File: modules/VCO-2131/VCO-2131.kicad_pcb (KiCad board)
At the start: 2 copper layers, 167.3 x 108.2 mm, 108 parts, among them J1 WQP-PJ398, J10 Conn_Front_Left, J11 Conn_Front_Right, J12 Conn_Back_Right, J13 Conn_Back_Left, J14 Conn_Passthru_Right, J15 Conn_Passthru_Left, J16 Conn_Mid_Right, J17 Conn_Mid_Left, J2 WQP-PJ398, J3 WQP-PJ398, J4 WQP-PJ398, J5 WQP-PJ398, J6 WQP-PJ398, J7 WQP-PJ398, J8 WQP-PJ398, J9 Conn_Eurorack_16, SW5 ON_OFF_ON, U1 L78L05, U2 L79L05, U3 LM4040, U4 SSI2131, U5 TL074, U6 TL074, U7 TL074, U8 CD4013

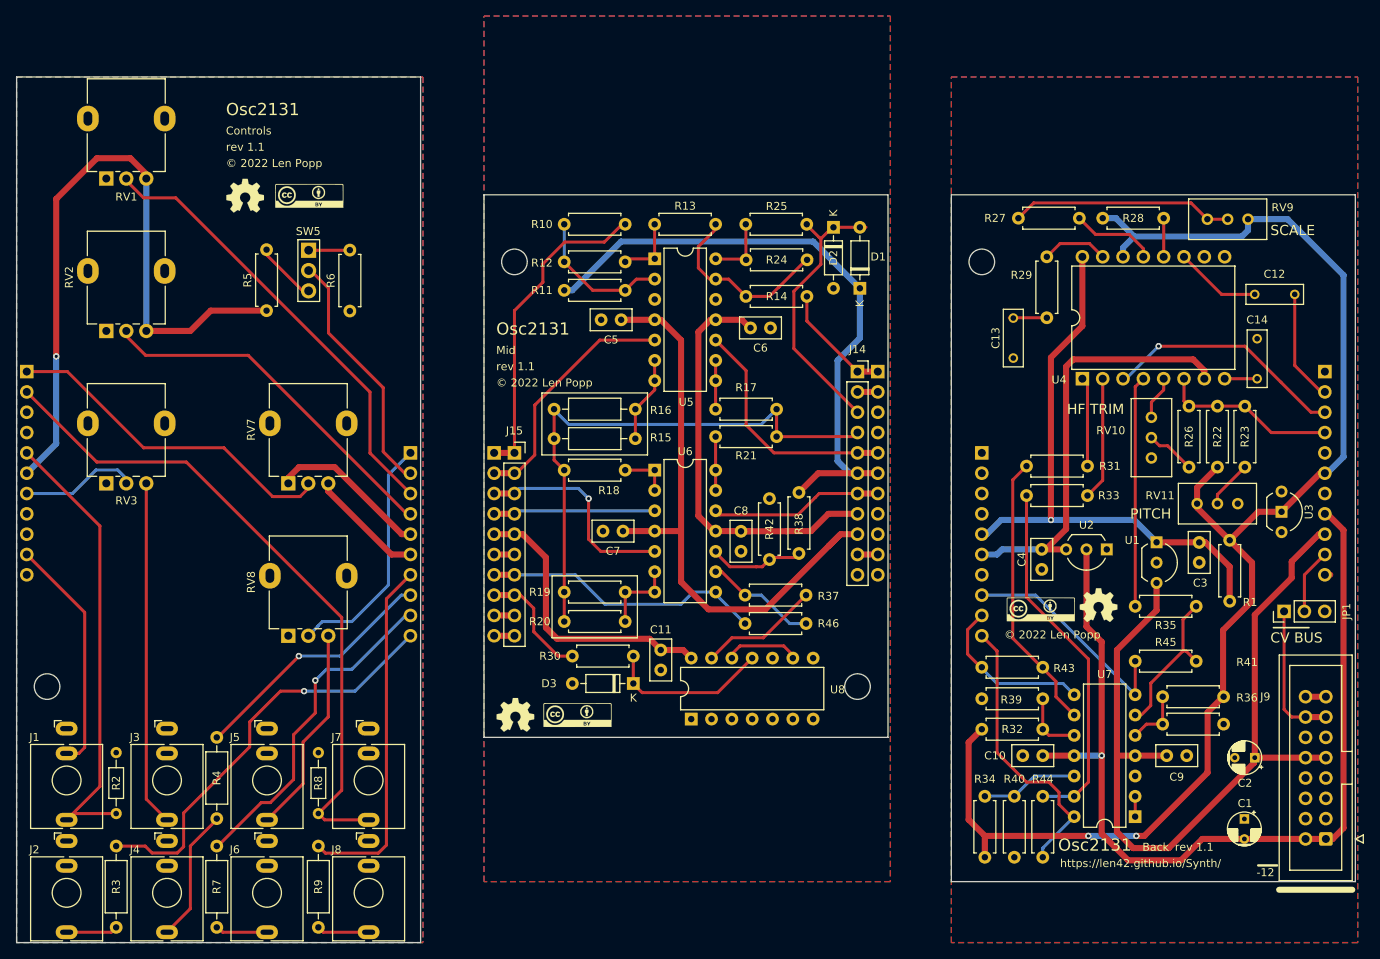
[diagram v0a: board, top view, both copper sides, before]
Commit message: VCO-2131: BOM cleanup, minor circuit changes, and footprint fixes
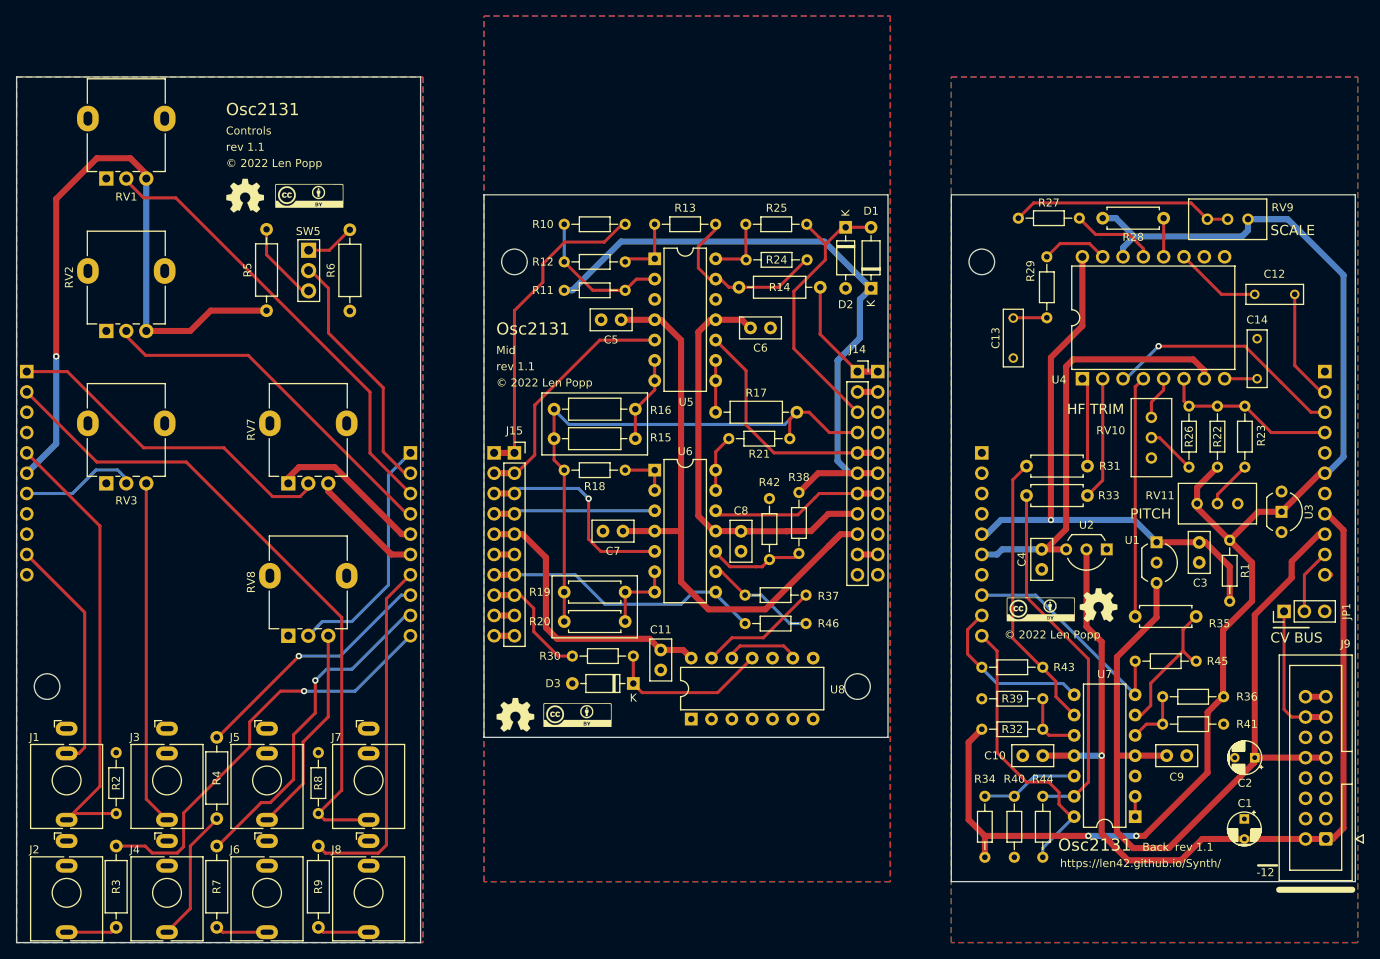
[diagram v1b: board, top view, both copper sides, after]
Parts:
- R1: value 1K -> 470R; footprint -lmp-misc:R_Axial_DIN0207_L6.3mm_D2.5mm_P7.62mm_Horizontal -> -lmp-misc:R_Axial_DIN0204_L3.6mm_D1.6mm_P7.62mm_Horizontal
- R10, R11, R12, R13, R18, R21, R22, R23, R24, R25, R26, R27, R29, R30, R32, R34, R36, R37, R38, R39, R40, R41, R42, R43, R44, R45, R46: footprint -lmp-misc:R_Axial_DIN0207_L6.3mm_D2.5mm_P7.62mm_Horizontal -> -lmp-misc:R_Axial_DIN0204_L3.6mm_D1.6mm_P7.62mm_Horizontal
- R14, R17, R5, R6: footprint -lmp-misc:R_Axial_DIN0207_L6.3mm_D2.5mm_P7.62mm_Horizontal -> -lmp-misc:R_Axial_DIN0207_L6.3mm_D2.5mm_P10.16mm_Horizontal
- R2: value 100K -> 4M7; footprint Resistor_THT:R_Axial_DIN0204_L3.6mm_D1.6mm_P7.62mm_Horizontal -> -lmp-misc:R_Axial_DIN0204_L3.6mm_D1.6mm_P7.62mm_Horizontal
- R8: footprint Resistor_THT:R_Axial_DIN0204_L3.6mm_D1.6mm_P7.62mm_Horizontal -> -lmp-misc:R_Axial_DIN0204_L3.6mm_D1.6mm_P7.62mm_Horizontal
- moved R17 2.57 mm to (121.7, 66.0)
- moved R21 1.67 mm to (120.8, 69.3)
- moved D2 1.52 mm to (127.8, 42.9)
- moved R14 1.44 mm to (114.4, 50.4)
- moved D1 1.40 mm to (130.9, 50.5)
- moved R35 1.27 mm to (171.6, 91.6)
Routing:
- net Net-(R5-Pad2): track 7.39 -> 9.93 mm
- net VREF+: track 337.4 -> 339.4 mm
- net Net-(R6-Pad2): track 4.83 -> 6.22 mm
- net Net-(R35-Pad1): track 18.6 -> 17.3 mm
- net Net-(R35-Pad2): track 28.9 -> 30.1 mm
- net PWM-2131: track 64.6 -> 65.9 mm
- net Net-(R13-Pad1): track 21.9 -> 21.0 mm
- net EXPO-FREQ-2131: track 92.3 -> 93.2 mm

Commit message: VCO-2131: PCB layout tweaks
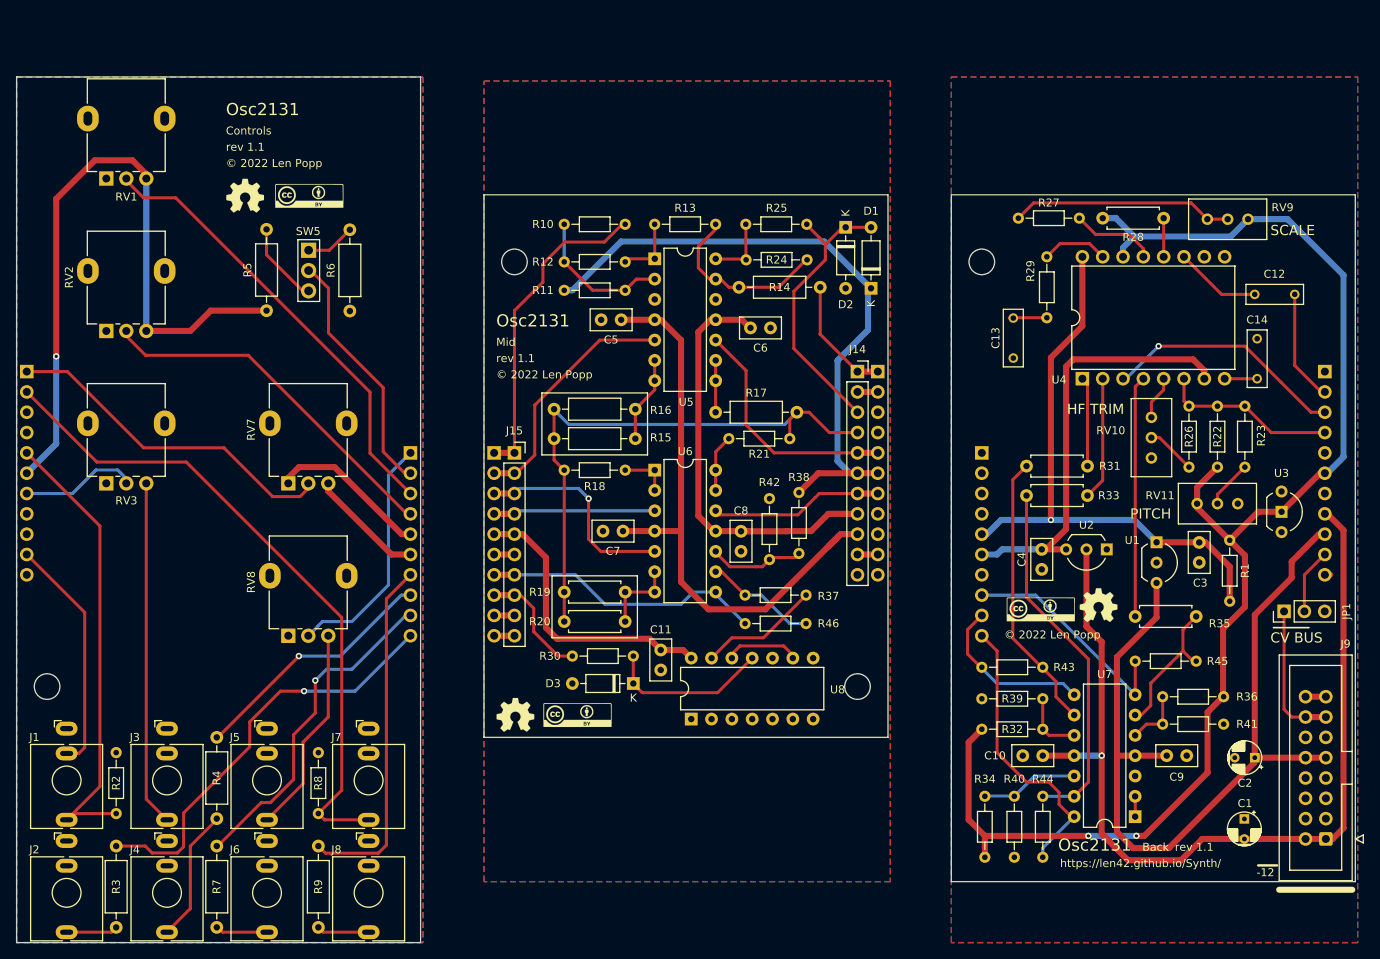
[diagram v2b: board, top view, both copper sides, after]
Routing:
- net VREF+: track 339.4 -> 337.6 mm
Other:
- board text removed: "TODO: Check all resistor footprints"
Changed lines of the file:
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@@
     (property "Value2" "2V5")
     (attr through_hole)
-    (fp_text reference "U3" (at 2.54 -3.43 -90) (layer "F.SilkS")
+    (fp_text reference "U3" (at -2.286 0) (layer "F.SilkS")
       (effects (font (size 1 1) (thickness 0.15)))
     )
@@
   (gr_line (start 191.470001 124.714) (end 140.97 124.714) (layer "Edge.Cuts") (width 0.1524))
   (gr_line (start 24.13 132.334) (end 24.13 24.13) (layer "Edge.Cuts") (width 0.1524))
-  (gr_text "© 2022 Len Popp" (at 84.074 62.357) (layer "F.SilkS")
+  (gr_text "© 2022 Len Popp" (at 84.074 61.341) (layer "F.SilkS")
     (effects (font (size 1 1) (thickness 0.15)) (justify left))
   )
-  (gr_text "Mid" (at 84.074 58.293) (layer "F.SilkS")
+  (gr_text "Mid" (at 84.074 57.277) (layer "F.SilkS")
     (effects (font (size 1 1) (thickness 0.15)) (justify left))
   )
@@
     (effects (font (size 1 1) (thickness 0.15)) (justify left))
   )
-  (gr_text "Osc2131" (at 84.074 55.626) (layer "F.SilkS")
+  (gr_text "Osc2131" (at 84.074 54.61) (layer "F.SilkS")
     (effects (font (size 1.524 1.524) (thickness 0.2286)) (justify left))
   )
@@
     (effects (font (size 1.27 1.27) (thickness 0.2032)) (justify left))
   )
-  (gr_text "rev 1.1" (at 84.074 60.325) (layer "F.SilkS")
-    (effects (font (size 1 1) (thickness 0.15)) (justify left))
-  )
-  (gr_text "TODO: Check all resistor footprints" (at 38.8874 136.652) (layer "Cmts.User")
+  (gr_text "rev 1.1" (at 84.074 59.309) (layer "F.SilkS")
     (effects (font (size 1 1) (thickness 0.15)) (justify left))
   )
@@
   (segment (start 153.416 79.502) (end 163.83 79.502) (width 0.762) (layer "B.Cu") (net 27))
   (segment (start 179.324 78.486) (end 175.768 82.042) (width 0.762) (layer "F.Cu") (net 28))
-  (segment (start 38.354 34.29) (end 40.34 36.276) (width 0.762) (layer "F.Cu") (net 28))
-  (segment (start 173 103.541) (end 174.941 101.6) (width 0.762) (layer "F.Cu") (net 28))
+  (segment (start 177.673 83.947) (end 175.768 82.042) (width 0.762) (layer "F.Cu") (net 28))
+  (segment (start 29.083 59.055) (end 29.083 39.37) (width 0.762) (layer "F.Cu") (net 28))
   (segment (start 174.234 72.898) (end 171.694 75.438) (width 0.762) (layer "F.Cu") (net 28))
+  (segment (start 29.083 39.37) (end 33.909 34.544) (width 0.762) (layer "F.Cu") (net 28))
   (segment (start 145.161 118.999) (end 145.161 121.666) (width 0.762) (layer "F.Cu") (net 28))
+  (segment (start 165.1 118.999) (end 173 111.099) (width 0.762) (layer "F.Cu") (net 28))
   (segment (start 48.387 53.34) (end 55.372 53.34) (width 0.762) (layer "F.Cu") (net 28))
   (segment (start 145.161 118.999) (end 143.129 116.967) (width 0.762) (layer "F.Cu") (net 28))
   (segment (start 143.129 107.315) (end 144.78 105.664) (width 0.762) (layer "F.Cu") (net 28))
-  (segment (start 34.163 34.29) (end 38.354 34.29) (width 0.762) (layer "F.Cu") (net 28))
-  (segment (start 173 111.099) (end 173 103.541) (width 0.762) (layer "F.Cu") (net 28))
-  (segment (start 178.562 84.836) (end 175.768 82.042) (width 0.762) (layer "F.Cu") (net 28))
   (segment (start 164.099 118.999) (end 165.1 118.999) (width 0.762) (layer "F.Cu") (net 28))
   (segment (start 45.847 55.88) (end 40.34 55.88) (width 0.762) (layer "F.Cu") (net 28))
-  (segment (start 40.34 36.276) (end 40.34 36.83) (width 0.762) (layer "F.Cu") (net 28))
   (segment (start 171.694 75.438) (end 171.694 77.47) (width 0.762) (layer "F.Cu") (net 28))
+  (segment (start 33.909 34.544) (end 38.608 34.544) (width 0.762) (layer "F.Cu") (net 28))
   (segment (start 129.24 73.66) (end 131.78 73.66) (width 0.762) (layer "F.Cu") (net 28))
+  (segment (start 40.34 36.276) (end 40.34 36.83) (width 0.762) (layer "F.Cu") (net 28))
+  (segment (start 173 111.099) (end 173 103.541) (width 0.762) (layer "F.Cu") (net 28))
+  (segment (start 174.941 101.6) (end 174.941 93.0925) (width 0.762) (layer "F.Cu") (net 28))
   (segment (start 121.92 76.073) (end 124.333 73.66) (width 0.762) (layer "F.Cu") (net 28))
-  (segment (start 174.941 101.6) (end 174.941 93.283) (width 0.762) (layer "F.Cu") (net 28))
   (segment (start 182.245 78.486) (end 179.324 78.486) (width 0.762) (layer "F.Cu") (net 28))
-  (segment (start 29.083 59.055) (end 29.083 39.37) (width 0.762) (layer "F.Cu") (net 28))
   (segment (start 158.1 118.999) (end 145.161 118.999) (width 0.762) (layer "F.Cu") (net 28))
+  (segment (start 173 103.541) (end 174.941 101.6) (width 0.762) (layer "F.Cu") (net 28))
   (segment (start 187.071 73.66) (end 182.245 78.486) (width 0.762) (layer "F.Cu") (net 28))
-  (segment (start 165.1 118.999) (end 173 111.099) (width 0.762) (layer "F.Cu") (net 28))
+  (segment (start 174.941 93.0925) (end 177.673 90.3605) (width 0.762) (layer "F.Cu") (net 28))
   (segment (start 187.66 73.66) (end 187.071 73.66) (width 0.762) (layer "F.Cu") (net 28))
-  (segment (start 178.562 89.662) (end 178.562 84.836) (width 0.762) (layer "F.Cu") (net 28))
+  (segment (start 38.608 34.544) (end 40.34 36.276) (width 0.762) (layer "F.Cu") (net 28))
   (segment (start 143.129 116.967) (end 143.129 107.315) (width 0.762) (layer "F.Cu") (net 28))
   (segment (start 171.694 77.968) (end 175.768 82.042) (width 0.762) (layer "F.Cu") (net 28))
-  (segment (start 29.083 39.37) (end 34.163 34.29) (width 0.762) (layer "F.Cu") (net 28))
-  (segment (start 174.941 93.283) (end 178.562 89.662) (width 0.762) (layer "F.Cu") (net 28))
   (segment (start 48.387 53.34) (end 45.847 55.88) (width 0.762) (layer "F.Cu") (net 28))
+  (segment (start 177.673 90.3605) (end 177.673 83.947) (width 0.762) (layer "F.Cu") (net 28))
   (segment (start 171.694 77.47) (end 171.694 77.968) (width 0.762) (layer "F.Cu") (net 28))
   (segment (start 124.333 73.66) (end 129.24 73.66) (width 0.762) (layer "F.Cu") (net 28))
@@
   (via (at 29.083 59.055) (size 0.8) (drill 0.4) (layers "F.Cu" "B.Cu") (net 28))
   (via (at 164.099 118.999) (size 0.8) (drill 0.4) (layers "F.Cu" "B.Cu") (net 28))
+  (segment (start 130.556 50.927) (end 130.556 55.753) (width 0.762) (layer "B.Cu") (net 28))
   (segment (start 99.695 44.704) (end 93.599 50.8) (width 0.762) (layer "B.Cu") (net 28))
   (segment (start 163.83 44.069) (end 162.433 45.466) (width 0.762) (layer "B.Cu") (net 28))
-  (segment (start 126.746 72.136) (end 128.27 73.66) (width 0.762) (layer "B.Cu") (net 28))
-  (segment (start 178.054 43.307) (end 177.292 44.069) (width 0.762) (layer "B.Cu") (net 28))
+  (segment (start 175.895 44.069) (end 163.83 44.069) (width 0.762) (layer "B.Cu") (net 28))
   (segment (start 183.007 41.91) (end 178.054 41.91) (width 0.762) (layer "B.Cu") (net 28))
   (segment (start 93.599 50.8) (end 92.583 50.8) (width 0.762) (layer "B.Cu") (net 28))
   (segment (start 162.433 45.466) (end 162.433 46.609) (width 0.762) (layer "B.Cu") (net 28))
+  (segment (start 126.746 72.136) (end 128.27 73.66) (width 0.762) (layer "B.Cu") (net 28))
   (segment (start 40.34 36.83) (end 40.34 55.88) (width 0.762) (layer "B.Cu") (net 28))
-  (segment (start 177.292 44.069) (end 163.83 44.069) (width 0.762) (layer "B.Cu") (net 28))
-  (segment (start 189.992 48.895) (end 183.007 41.91) (width 0.762) (layer "B.Cu") (net 28))
   (segment (start 128.27 73.66) (end 129.24 73.66) (width 0.762) (layer "B.Cu") (net 28))
-  (segment (start 129.54 56.769) (end 126.746 59.563) (width 0.762) (layer "B.Cu") (net 28))
-  (segment (start 178.054 41.91) (end 178.054 43.307) (width 0.762) (layer "B.Cu") (net 28))
+  (segment (start 189.992 48.895) (end 183.007 41.91) (width 0.762) (layer "B.Cu") (net 28))
   (segment (start 125.095 44.704) (end 99.695 44.704) (width 0.762) (layer "B.Cu") (net 28))
-  (segment (start 130.937 50.546) (end 129.54 51.943) (width 0.762) (layer "B.Cu") (net 28))
+  (segment (start 130.556 55.753) (end 126.746 59.563) (width 0.762) (layer "B.Cu") (net 28))
   (segment (start 187.96 73.66) (end 189.992 71.628) (width 0.762) (layer "B.Cu") (net 28))
   (segment (start 163.83 44.069) (end 161.544 41.783) (width 0.762) (layer "B.Cu") (net 28))
@@
   (segment (start 189.992 71.628) (end 189.992 48.895) (width 0.762) (layer "B.Cu") (net 28))
   (segment (start 29.083 69.977) (end 25.4 73.66) (width 0.762) (layer "B.Cu") (net 28))
+  (segment (start 178.054 41.91) (end 175.895 44.069) (width 0.762) (layer "B.Cu") (net 28))
+  (segment (start 126.746 59.563) (end 126.746 72.136) (width 0.762) (layer "B.Cu") (net 28))
   (segment (start 187.66 73.66) (end 187.96 73.66) (width 0.762) (layer "B.Cu") (net 28))
-  (segment (start 129.54 51.943) (end 129.54 56.769) (width 0.762) (layer "B.Cu") (net 28))
+  (segment (start 130.937 50.546) (end 130.556 50.927) (width 0.762) (layer "B.Cu") (net 28))
   (segment (start 164.099 118.999) (end 158.1 118.999) (width 0.762) (layer "B.Cu") (net 28))
-  (segment (start 126.746 59.563) (end 126.746 72.136) (width 0.762) (layer "B.Cu") (net 28))
   (segment (start 161.544 41.783) (end 159.893 41.783) (width 0.762) (layer "B.Cu") (net 28))
   (segment (start 29.083 59.055) (end 29.083 69.977) (width 0.762) (layer "B.Cu") (net 28))
@@
         (xy 133.35 124.714)
         (xy 82.55 124.714)
-        (xy 82.55 16.51)
-        (xy 133.35 16.51)
+        (xy 82.55 24.638)
+        (xy 133.35 24.638)
       )
     )
@@
         (xy 133.35 124.714)
         (xy 82.55 124.714)
-        (xy 82.55 16.51)
-        (xy 133.35 16.51)
+        (xy 82.55 24.638)
+        (xy 133.35 24.638)
       )
     )
